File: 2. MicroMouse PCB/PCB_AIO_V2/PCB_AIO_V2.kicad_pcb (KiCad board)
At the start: 2 copper layers, 60 x 73.8 mm, 44 parts, among them J1 Conn_01x02_Pin, J2 Conn_01x09_Pin, J3 MPU, J4 STLINK, J5 Conn_01x06_Pin, J6 Conn_01x06_Pin, J7 MPU, Q1 S8550, SW1 SW_Push, SW2 SW_Push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

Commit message: completed PCB_AIO_V2
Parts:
- added C19: 330uF, Capacitor_Tantalum_SMD:CP_EIA-7343-20_Kemet-V, B.Cu at (144.9, 119.5)
- added C20: 10uF, Capacitor_Tantalum_SMD:CP_EIA-3216-10_Kemet-I, F.Cu at (142.1, 114.7)
- added C21: 10uF, Capacitor_Tantalum_SMD:CP_EIA-3216-10_Kemet-I, F.Cu at (140.1, 124.3)
- added RN2: R_Pack05, Resistor_SMD:R_Array_Convex_5x0603, B.Cu at (143.6, 102.4)
- added SW4: SW_DIP_x05, Button_Switch_SMD:SW_DIP_SPSTx05_Slide_KingTek_DSHP05TS_W7.62mm_P1.27mm, F.Cu at (142.8, 102.1)
- added SW5: SW_DPDT_x2, Button_Switch_SMD:SW_SPDT_PCM12, F.Cu at (151.3, 132.0)
- added U3: AMS1117-3.3, Package_TO_SOT_SMD:SOT-223-3_TabPin2, F.Cu at (141.9, 119.5)
- C13, C16, C2, C3, J2, U4: moved to B.Cu
- J1: value Conn_01x02_Pin -> EN pin; footprint Connector_JST:JST_VH_B2P-VH-B_1x02_P3.96mm_Vertical -> Connector_PinHeader_2.54mm:PinHeader_1x01_P2.54mm_Vertical
- J3, J4: footprint JST254:JST 4 -> Connector_JST:JST_SH_BM04B-SRSS-TB_1x04-1MP_P1.00mm_Vertical; moved to F.Cu
- J5, J6: footprint JST254:JST 6 -> Connector_JST:JST_SH_BM06B-SRSS-TB_1x06-1MP_P1.00mm_Vertical
- moved D4 66.2 mm to (161.3, 69.7), turned to -90 degrees
- moved D3 62.7 mm to (163.9, 69.7), turned to -90 degrees
- moved D2 59.2 mm to (166.5, 69.7), turned to -90 degrees
- moved D1 55.8 mm to (169.1, 69.7), turned to -90 degrees
- moved J2 47.0 mm to (154.9, 75.0), turned to -90 degrees
- moved BZ1 45.3 mm to (184.9, 117.5)
- moved C4 43.5 mm to (177.8, 88.1), turned to 180 degrees
- moved Y1 38.2 mm to (151.6, 90.3)
- moved J4 36.4 mm to (183.5, 93.1), turned to -90 degrees
- moved C17 33.2 mm to (152.2, 87.6)
- moved C7 32.1 mm to (152.2, 86.0)
- moved C15 30.8 mm to (148.5, 90.6), turned to -90 degrees
- moved U4 30.6 mm to (165.1, 105.6), turned to -90 degrees
- moved RN1 29.7 mm to (165.3, 66.1), turned to 90 degrees
- moved J1 29.5 mm to (144.8, 125.9)
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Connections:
- net /RIGHT_MOTOR_01 renamed /RIGHT_MOTOR_O1
- D1 pad 2: /LED_3 -> /LED_0
- D2 pad 2: /LED_2 -> /LED_1
- D3 pad 2: /LED_1 -> /LED_2
- D4 pad 2: /LED_0 -> /LED_3
- J1 pad 1: /IN+ -> Net-(J1-Pin_1)
- J6 pad 6: /RIGHT_MOTOR_02 -> /RIGHT_MOTOR_O2
- Q1 pad 1: +3.3V -> +5V
- RN1 pad 1: Net-(D1-K) -> Net-(D4-K)
- RN1 pad 2: Net-(D2-K) -> Net-(D3-K)
- RN1 pad 3: Net-(D3-K) -> Net-(D2-K)
- RN1 pad 4: Net-(D4-K) -> Net-(D1-K)
- U1 pad 1: /LED_0 -> /BIT_SW_0
- U1 pad 15: /IR_SENSOR_BL -> /IR_SENSOR_FR
- U1 pad 16: /IR_SENSOR_BR -> /IR_SENSOR_RR
- U1 pad 2: /LED_1 -> /BIT_SW_1
- U1 pad 24: /IR_SENSOR_RR -> /IR_SENSOR_BR
- U1 pad 25: /IR_SENSOR_FR -> /IR_SENSOR_BL
- U1 pad 3: /LED_2 -> /BIT_SW_2
- U1 pad 30: /IR_SENSOR_FF -> /IR_SENSOR_RL
- U1 pad 35: /IR_SENSOR_RL -> /IR_SENSOR_FF
- U1 pad 4: /LED_3 -> /BIT_SW_3
- U1 pad 5: unconnected-(U1-PE6-Pad5) -> /BIT_SW_4
- U1 pad 81: unconnected-(U1-PD0-Pad81) -> /LED_0
- U1 pad 82: unconnected-(U1-PD1-Pad82) -> /LED_1
- U1 pad 83: unconnected-(U1-PD2-Pad83) -> /LED_2
- U1 pad 84: unconnected-(U1-PD3-Pad84) -> /LED_3
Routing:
- net +3.3V: track 0.00 -> 258.8 mm, vias 0 -> 17
- net /BUTTON_0: track 0.00 -> 91.7 mm, vias 0 -> 2
- net /BUTTON_1: track 0.00 -> 86.1 mm, vias 0 -> 2
- net +5V: track 0.00 -> 81.9 mm, vias 0 -> 4
- net /IR_SENSOR_FF: track 0.00 -> 52.4 mm
- net /IR_SENSOR_FL: track 0.00 -> 51.9 mm
- net /IR_SENSOR_RL: track 0.00 -> 51.9 mm
- net /IR_SENSOR_FR: track 0.00 -> 49.3 mm
- net /IR_SENSOR_BR: track 0.00 -> 48.1 mm
- net /IR_SENSOR_RR: track 0.00 -> 48.0 mm
- net /IR_SENSOR_BL: track 0.00 -> 46.8 mm
- net /NRST: track 0.00 -> 39.6 mm, vias 0 -> 2
- net /LED_3: track 0.00 -> 37.0 mm
- net /LED_2: track 0.00 -> 34.8 mm
- net /USART2_RX: track 0.00 -> 33.6 mm, vias 0 -> 2
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- added copper zone on B.Cu, net +5V
- added copper zone on B.Cu, net GND
- added copper zone on F.Cu, net GND
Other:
- board size 60 x 73.8 mm -> 60 x 72 mm
- board text added: "5V"
- board text added: "BL"
- board text added: "BR"
- board text added: "DISPLAY"
- board text added: "FF"
- board text added: "FL"
- board text added: "FR"
- board text added: "G"
- board text added: "GND"
- board text added: "IR SENSOR"
- board text added: "LEFT MOTOR"
- board text added: "MPU"
- board text added: "RESET"
- board text added: "RIGHT MOTOR"
- board text added: "RL"
- board text added: "RR"
- board text added: "RX"
- board text added: "ST-LINK"
- board text added: "SW0"
- board text added: "SW1"
- board text added: "TX"
- board text added: "VCC"

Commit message: updated logo AML
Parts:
- added G***: LOGO, LOGO, F.Cu at (150.9, 118.5)

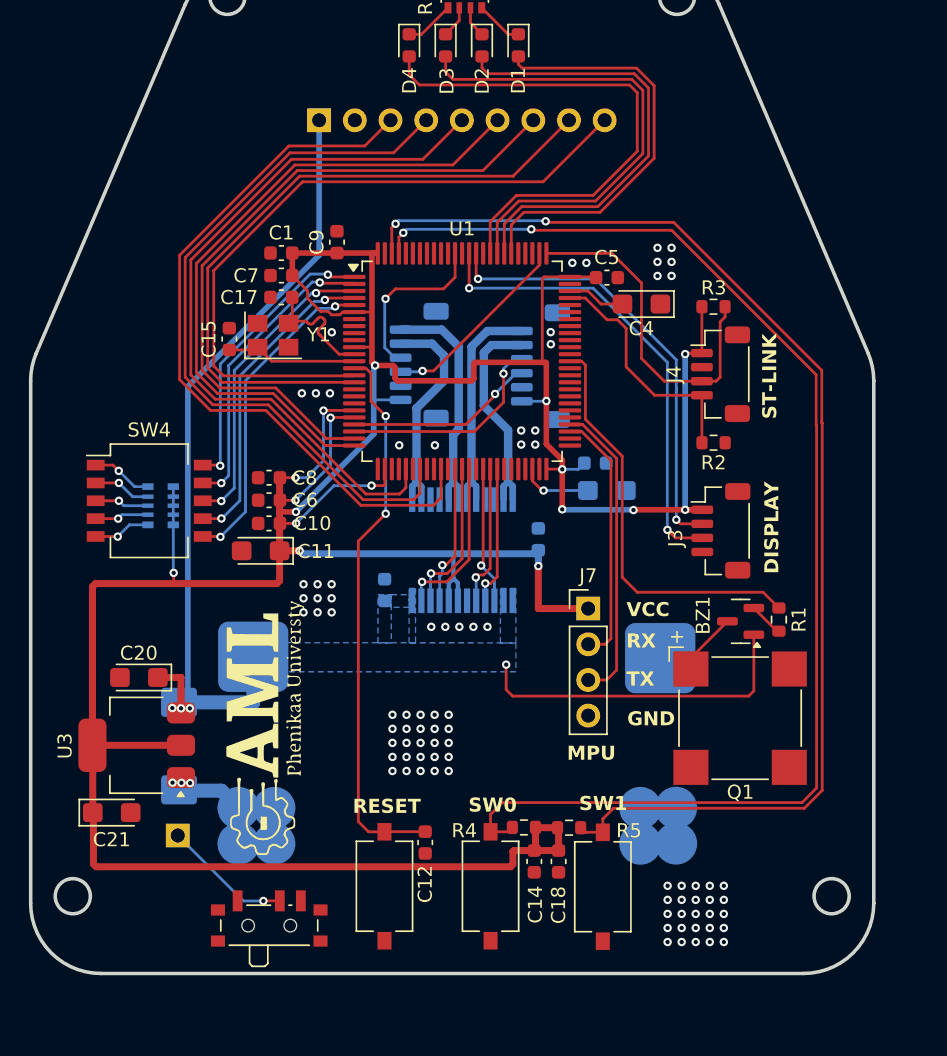
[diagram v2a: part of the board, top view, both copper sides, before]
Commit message: SH 1.0 4P -> XH 2.54 4P
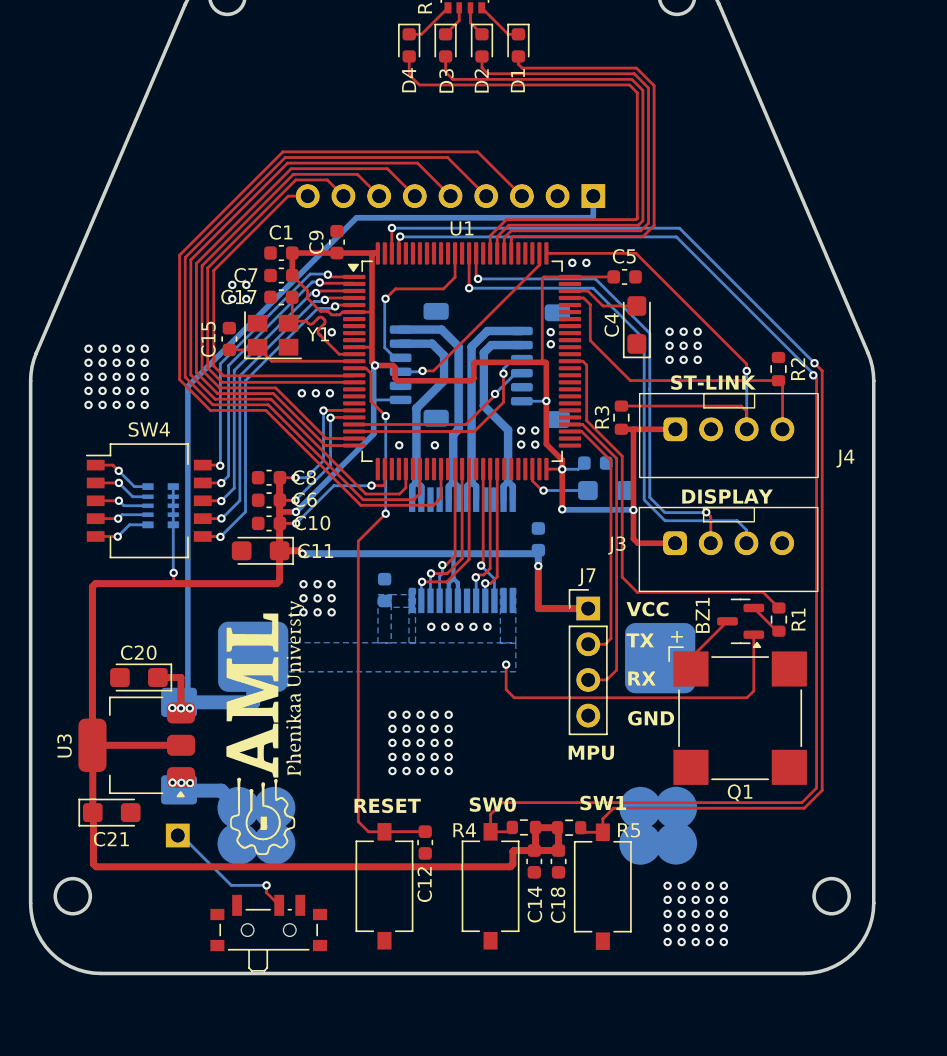
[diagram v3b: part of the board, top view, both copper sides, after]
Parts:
- J3, J4: footprint Connector_JST:JST_SH_BM04B-SRSS-TB_1x04-1MP_P1.00mm_Vertical -> JST254:JST 4
- moved J2 20.2 mm to (174.4, 80.4), turned to 90 degrees
- moved R3 10.3 mm to (176.4, 96.2), turned to -90 degrees
- moved J4 8.69 mm to (177.7, 99.6), turned to 0 degrees
- moved R2 6.99 mm to (187.6, 92.7), turned to -90 degrees
- moved J3 6.76 mm to (177.7, 107.7), turned to 0 degrees
- moved C4 1.52 mm to (177.5, 89.6), turned to 90 degrees
- moved C5 1.26 mm to (176.6, 86.2)
- moved SW5 0.32 mm to (151.3, 132.3)
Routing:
- net /IR_SENSOR_FR: track 49.3 -> 26.0 mm
- net /IR_SENSOR_RR: track 48.0 -> 30.7 mm
- net +5V: track 81.9 -> 94.5 mm
- net /IR_SENSOR_BR: track 48.1 -> 36.2 mm
- net /IR_SENSOR_FF: track 52.4 -> 62.1 mm
- net /SWCLK: track 24.6 -> 32.5 mm, vias 0 -> 1
- net /IR_SENSOR_BL: track 46.8 -> 40.3 mm
- net /SWDIO: track 17.2 -> 22.4 mm
- net +3.3V: track 258.8 -> 254.2 mm, vias 17 -> 15
- net /IR_SENSOR_FL: track 51.9 -> 56.2 mm
- net /USART2_RX: track 33.6 -> 37.1 mm, vias 2 -> 1
- net /USART2_TX: track 31.9 -> 34.2 mm
- net /LED_1: track 32.4 -> 34.7 mm
- net /LED_0: track 30.2 -> 32.4 mm
- net /LED_3: track 37.0 -> 39.2 mm
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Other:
- board text added: "3.3"
- board text added: "CLK"
- board text added: "DIO"

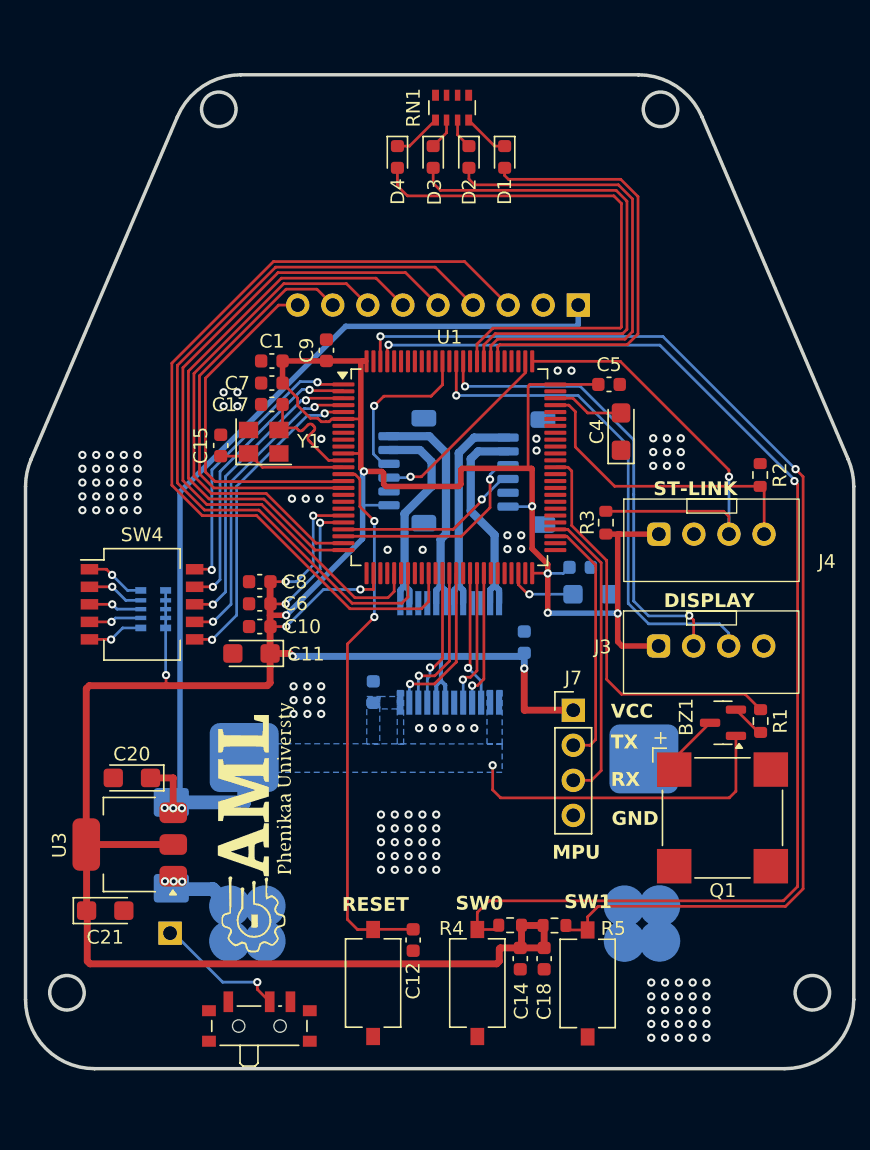
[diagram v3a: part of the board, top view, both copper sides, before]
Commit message: completed PCB_AIO_V2 pin config
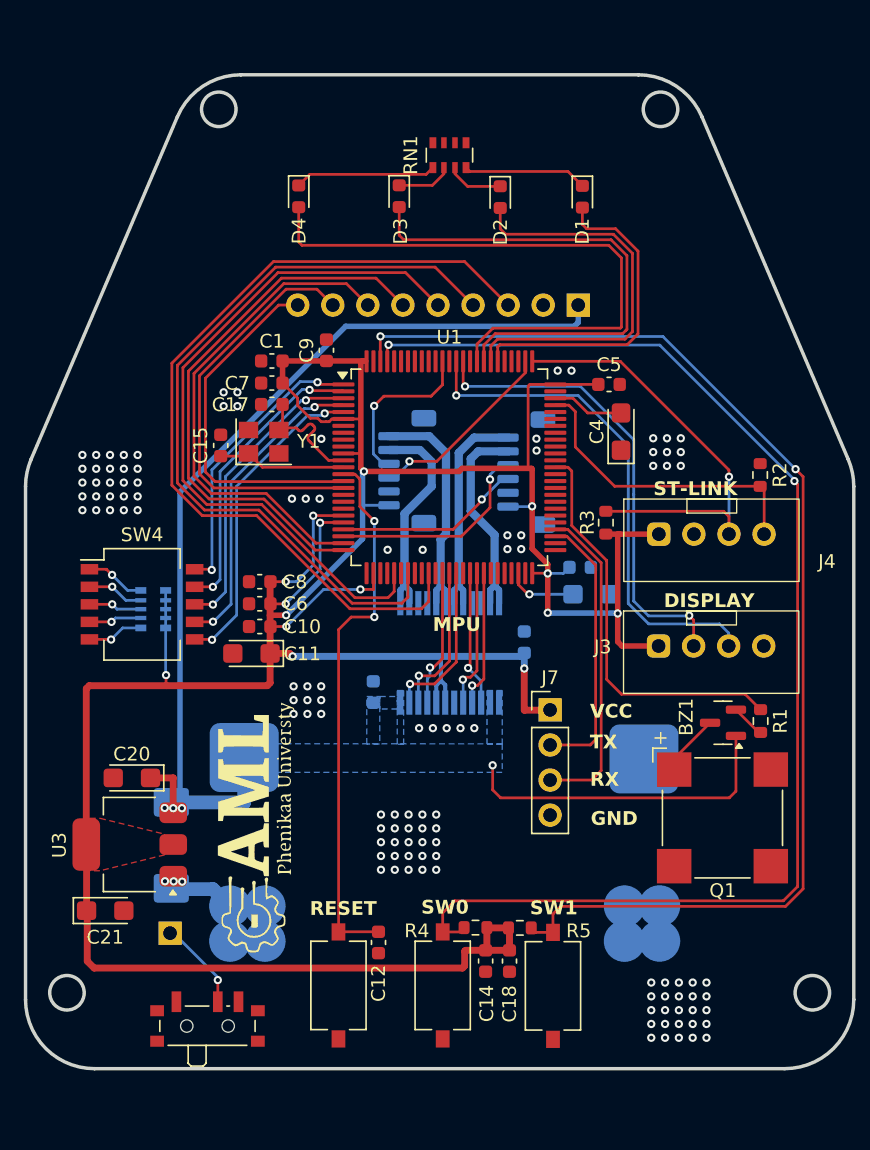
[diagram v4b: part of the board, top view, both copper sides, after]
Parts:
- moved D4 7.70 mm to (154.2, 72.5)
- moved D1 6.32 mm to (174.7, 72.6)
- moved SW5 3.76 mm to (147.6, 132.3)
- moved D3 3.76 mm to (161.4, 72.5)
- moved D2 3.69 mm to (168.8, 72.6)
- moved RN1 3.45 mm to (165.1, 69.5)
- moved SW1 2.52 mm to (157.0, 129.7)
- moved C14 2.52 mm to (167.7, 127.9)
- moved SW2 2.52 mm to (164.6, 129.7)
- moved SW3 2.52 mm to (172.6, 129.7)
- moved C12 2.52 mm to (159.9, 126.6)
- moved C18 2.52 mm to (169.4, 127.9)
- moved R4 2.52 mm to (167.0, 125.5)
- moved R5 2.52 mm to (170.2, 125.5)
- moved J7 1.68 mm to (172.4, 109.7)
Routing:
- net +3.3V: track 254.2 -> 242.1 mm
- net /LED_0: track 32.4 -> 23.7 mm
- net Net-(D4-K): track 3.54 -> 10.3 mm
- net Net-(D1-K): track 3.39 -> 8.98 mm
- net /LED_1: track 34.7 -> 29.3 mm
- net /LED_3: track 39.2 -> 43.6 mm
- net Net-(J1-Pin_1): track 9.58 -> 6.56 mm
- net /BUTTON_1: track 85.6 -> 88.4 mm
- net /BUTTON_0: track 91.1 -> 93.8 mm
- net Net-(D2-K): track 2.22 -> 4.11 mm
- net Net-(D3-K): track 2.29 -> 4.03 mm
- net /USART1_TX: track 18.2 -> 19.9 mm
- net /USART1_RX: track 21.7 -> 23.4 mm
- added copper zone on F.Cu, net +3.3V
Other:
- board text added: "PCB_AIO_V2"
- board text added: "QUỶ ĐỎ 1"
